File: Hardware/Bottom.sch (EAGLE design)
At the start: 13 parts, among them IC1 SI570, IC2 74LVC74A, X1 MINI-USB-SCHIELD-32005-201

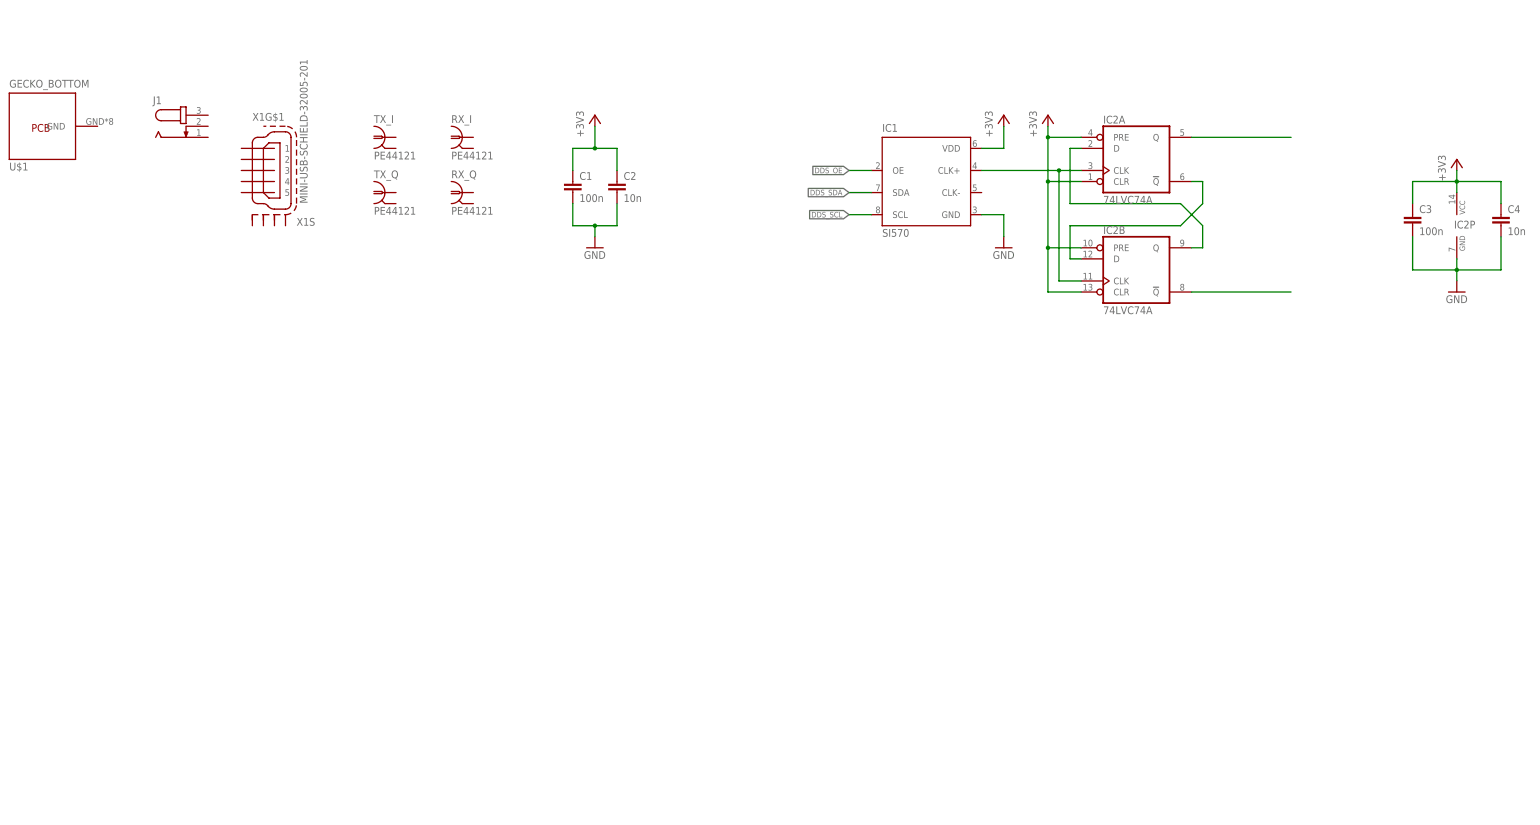
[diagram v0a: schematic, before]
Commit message: Add stepdown converters
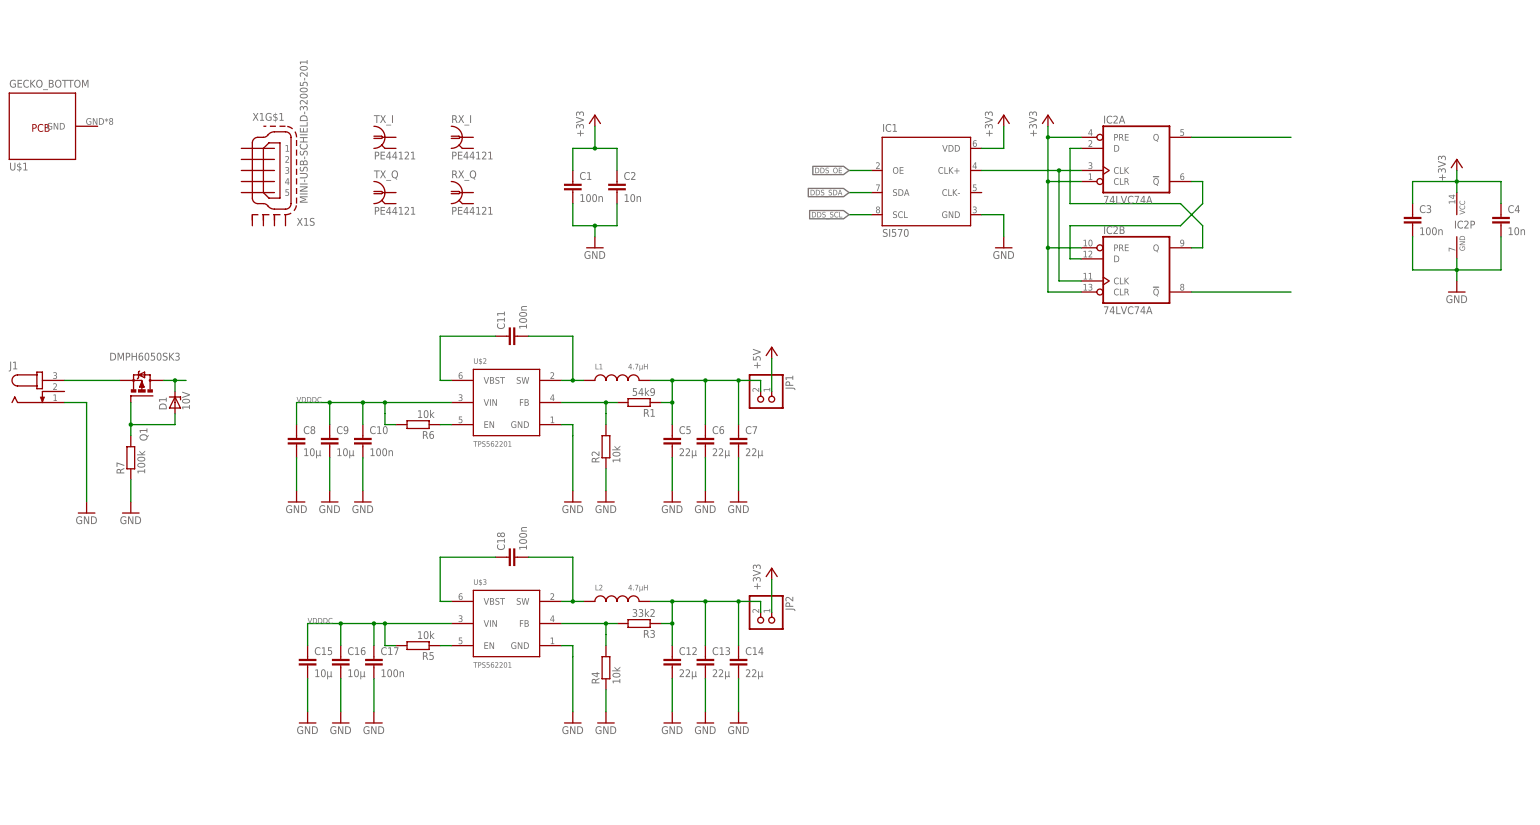
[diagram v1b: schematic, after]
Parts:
- added C10, C11, C17, C18: 100n, rcl:C-EUC0603
- added C12, C13, C14, C5, C6, C7: 22µ, rcl:C-EUC0805
- added C15, C16, C8, C9: 10µ, rcl:C-EUC0805
- added D1: 10V, diode:ZENER-DIODESOT23
- added JP1, JP2: (no value), pinhead:PINHD-1X2
- added L1, L2: 4.7µH, PowerMagnetics (rev18d):WE-MAPI_3020_74438336047
- added Q1: DMPH6050SK3, MyLib:DMP3099L
- added R1: 54k9, rcl:R-EU_R0603
- added R2, R4: 10k, rcl:R-EU_R0603
- added R3: 33k2, rcl:R-EU_R0603
- added R5, R6: 10k, rcl:R-EU_R0402
- added R7: 100k, rcl:R-EU_R0402
- added U$2, U$3: TPS562201, MyLib:TPS562201
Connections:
- new net +5V: JP1.1
- new net N$10: D1.C, Q1.D
- new net N$11: R1.2, R2.2, U$2.FB
- new net N$12: J1.3, Q1.S
- new net N$15: C18.1, U$3.VBST
- new net N$19: C18.2, L2.1, U$3.SW
- new net N$20: R3.2, R4.2, U$3.FB
- new net N$30: C5.1, C6.1, C7.1, JP1.2, L1.2, R1.1
- new net N$31: C12.1, C13.1, C14.1, JP2.2, L2.2, R3.1
- new net N$7: C11.1, U$2.VBST
- new net N$8: C11.2, L1.1, U$2.SW
- new net N$9: D1.A, Q1.G, R7.2
- new net VDDDC: C10.1, C15.1, C16.1, C17.1, C8.1, C9.1, R5.2, R6.2, U$2.VIN, U$3.VIN
- new net VREG_VDD3V3_EN: R5.1, U$3.EN
- new net VREG_VDD5_EN: R6.1, U$2.EN
- net +3V3: now also JP2.1
- net GND: now also C10.2, C12.2, C13.2, C14.2, C15.2, C16.2, C17.2, C5.2, C6.2, C7.2, C8.2, C9.2, J1.1, R2.1, R4.1, R7.1, U$2.GND, U$3.GND
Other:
- moved on the sheet: J1

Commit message: Add sides, add Tayloe Detector
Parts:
- removed RX_I, RX_Q, TX_I, TX_Q: PE44121, con-coax:PE44121
- removed X1: MINI-USB-SCHIELD-32005-201, con-cypressindustries:MINI-USB-SCHIELD-32005-201
- added C19, C20, C21, C26, C27, C31: 100n, rcl:C-EUC0603
- added C22, C23, C24, C25: 4µ7, rcl:C-EUC0805
- added C28: 1µ, rcl:C-EUC0603
- added C29, C30: 2µ, rcl:C-EUC0805
- added C32, C33, C34, C35: (no value), rcl:C-EUC1210
- added C36, C37, C38, C39: (no value), rcl:C-EUC0603
- added IC5: LT6232CGN, linear-technology:LT6232CGN
- added L3, L4: 33µ, rcl:L-EUL3216C
- added R10, R11, R14, R15, R16, R17, R18, R9: (no value), rcl:R-EU_R0603
- added R12, R13: 10k, rcl:R-EU_M0805
- added R8: 10k, rcl:R-EU_R0603
- added RX_IN, RX_IN1: PE44121, con-coax:PE44121
- added SV3, SV4: (no value), con-lstb:MA05-2
- added U$4, U$5: TMUX1511TSSOP14, MyLib:TMUX1511TSSOP14
- added U$6: MABA-007237-ETC410, MyLib:MABA-007237-ETC410
- added U$7: ADS7946, MyLib:ADS7946
- added U$8: MCP1501, MyLib:MCP1501
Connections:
- net DDS_SCL renamed I2C_OSC_SCL
- net DDS_SDA renamed I2C_OSC_SDA
- removed net DDS_OE: IC1.OE
- removed net VDDDC: C10.1, C15.1, C16.1, C17.1, C8.1, C9.1, R5.2, R6.2, U$2.VIN, U$3.VIN
- new net ADC_CHSEL: SV4.1, U$7.CHSEL
- new net I2C_MCS_SCL: SV3.9
- new net I2C_MCS_SDA: SV3.10
- new net N$13: C37.1, IC5D.+IN, R14.2
- new net N$14: IC5A.OUT, R9.1
- new net N$16: C21.1, RX_IN.1
- new net N$17: C21.2, U$6.PD
- new net N$18: C22.1, C23.1, C24.1, C25.1, L3.1, R12.2, U$6.CT
- new net N$21: L3.2, R13.1
- new net N$22: U$4.D1, U$4.D2, U$4.D3, U$4.D4, U$6.SD
- new net N$23: U$5.D1, U$5.D2, U$5.D3, U$5.D4, U$6.S
- new net N$24: C32.1, IC5A.+IN, U$4.S1, U$5.S3
- new net N$25: U$7.A1INP
- new net N$26: U$7.A1INN
- new net N$27: U$7.AREF, U$8.OUT
- new net N$28: U$7.A0INN
- new net N$29: C27.1, C28.1, C29.1, L4.2, U$7.AVDD, U$8.!SHDN, U$8.VDD
- new net N$32: U$7.A0INP
- new net N$33: C33.1, IC5B.+IN, U$4.S2, U$5.S4
- new net N$34: C34.1, IC5A.-IN, U$4.S3, U$5.S1
- new net N$35: SV4.10
- new net N$36: SV4.8
- new net N$37: SV4.6
- new net N$38: SV4.4
- new net N$39: C35.1, IC5B.-IN, U$4.S4, U$5.S2
- new net N$40: C38.1, R10.1, R9.2
- new net N$41: C36.1, IC5C.+IN, R10.2
- new net N$42: C38.2, IC5C.OUT, R18.1
- new net N$43: C39.2, IC5D.OUT, R16.1
- new net N$44: IC5D.-IN, R15.2, R16.2
- new net N$45: IC5C.-IN, R17.2, R18.2
- new net N$6: IC5B.OUT, R11.1
- new net RESV_NC: SV4.2
- new net SPI_ADC_MISO: R8.1, U$7.SDO
- new net SPI_MCS_CLK: SV4.9, U$7.SCLK
- new net SPI_MCS_CS: SV4.3, U$7.!CS
- new net SPI_MCS_MISO: R8.2, SV4.5
- new net SPI_MCS_MOSI: SV4.7
- new net VDD_DC: C10.1, C15.1, C16.1, C17.1, C8.1, C9.1, D1.C, Q1.D, R5.2, R6.2, U$2.VIN, U$3.VIN
- net +3V3: now also C19.1, C20.1, C30.1, C31.1, R13.2, SV3.6, SV3.8, U$4.VCC, U$5.VCC, U$7.DVDD
- net +5V: now also C26.1, IC5P.V+, SV3.2, SV3.4
- net GND: now also C19.2, C20.2, C22.2, C23.2, C24.2, C25.2, C26.2, C27.2, C28.2, C29.2, C30.2, C31.2, C32.2, C33.2, C34.2, C35.2, C36.2, C37.2, IC5P.V-, R12.1, R15.1, R17.1, RX_IN.2, RX_IN1.2, SV3.1, SV3.3, SV3.5, SV3.7, U$4.GND, U$5.GND, U$6.P, U$7.GND, U$7.NC@1, U$7.NC@2, U$7.PDEN, U$7.REFGND, U$8.GND@1, U$8.GND@2, U$8.GND@3
- net N$10: now also C39.1, R11.2, R14.1; no longer D1.C, Q1.D
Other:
- note added: "ECH-U1H153GX5 15nF PPS Film"

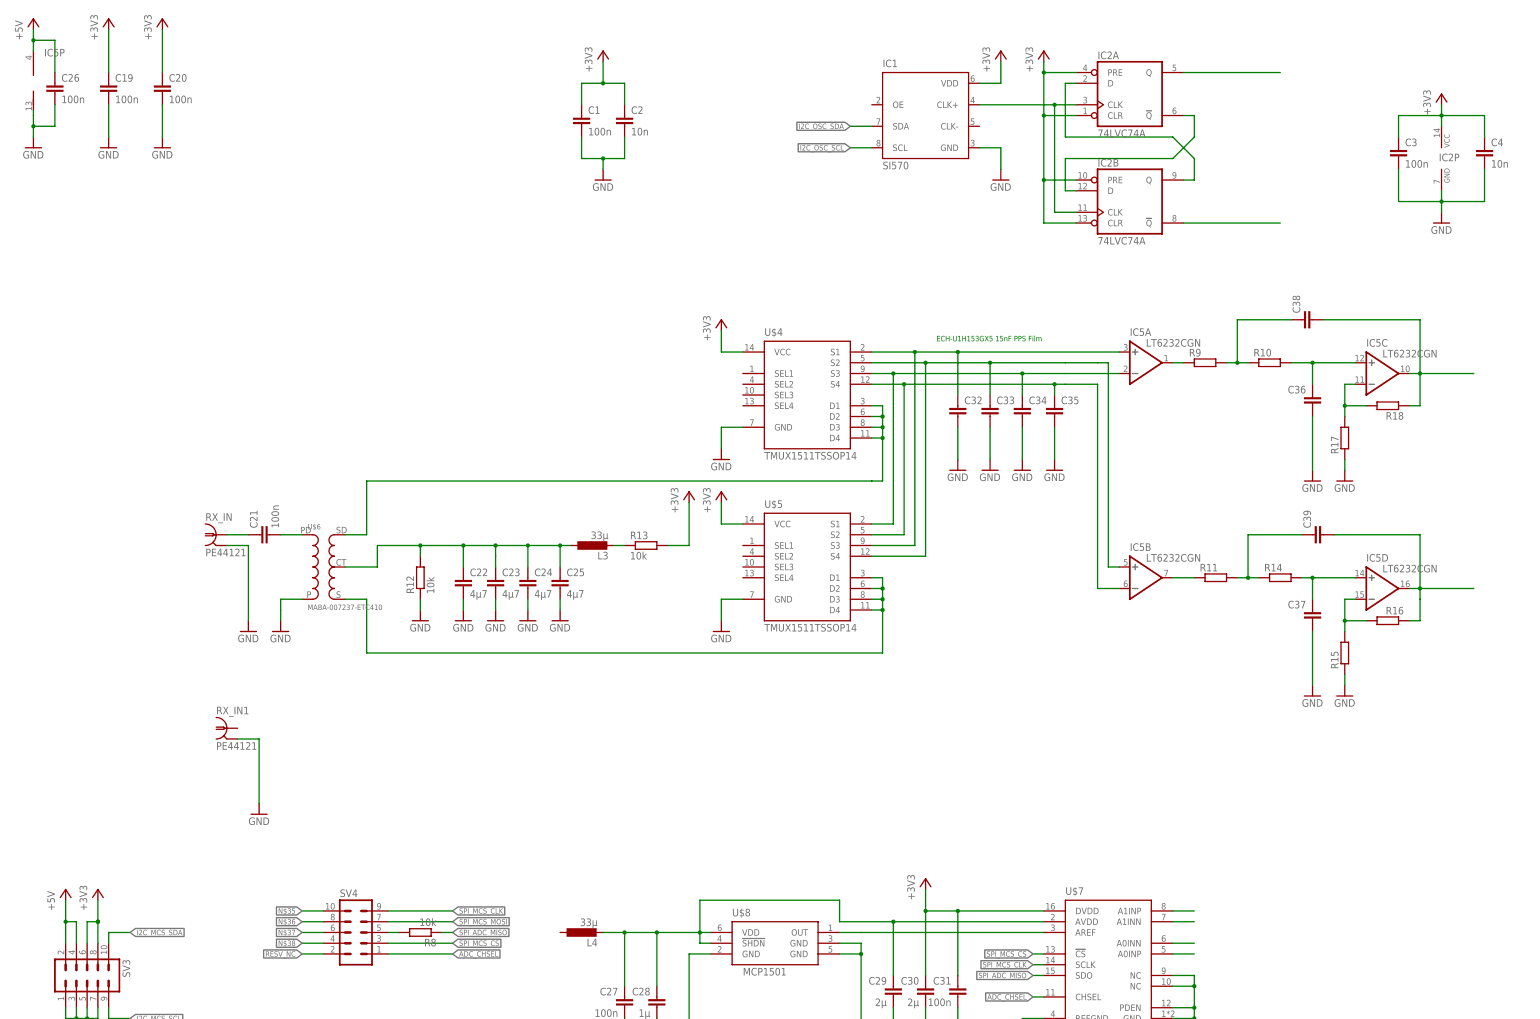
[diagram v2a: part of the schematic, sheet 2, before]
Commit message: Adds SN74CBT3253 to Bottom
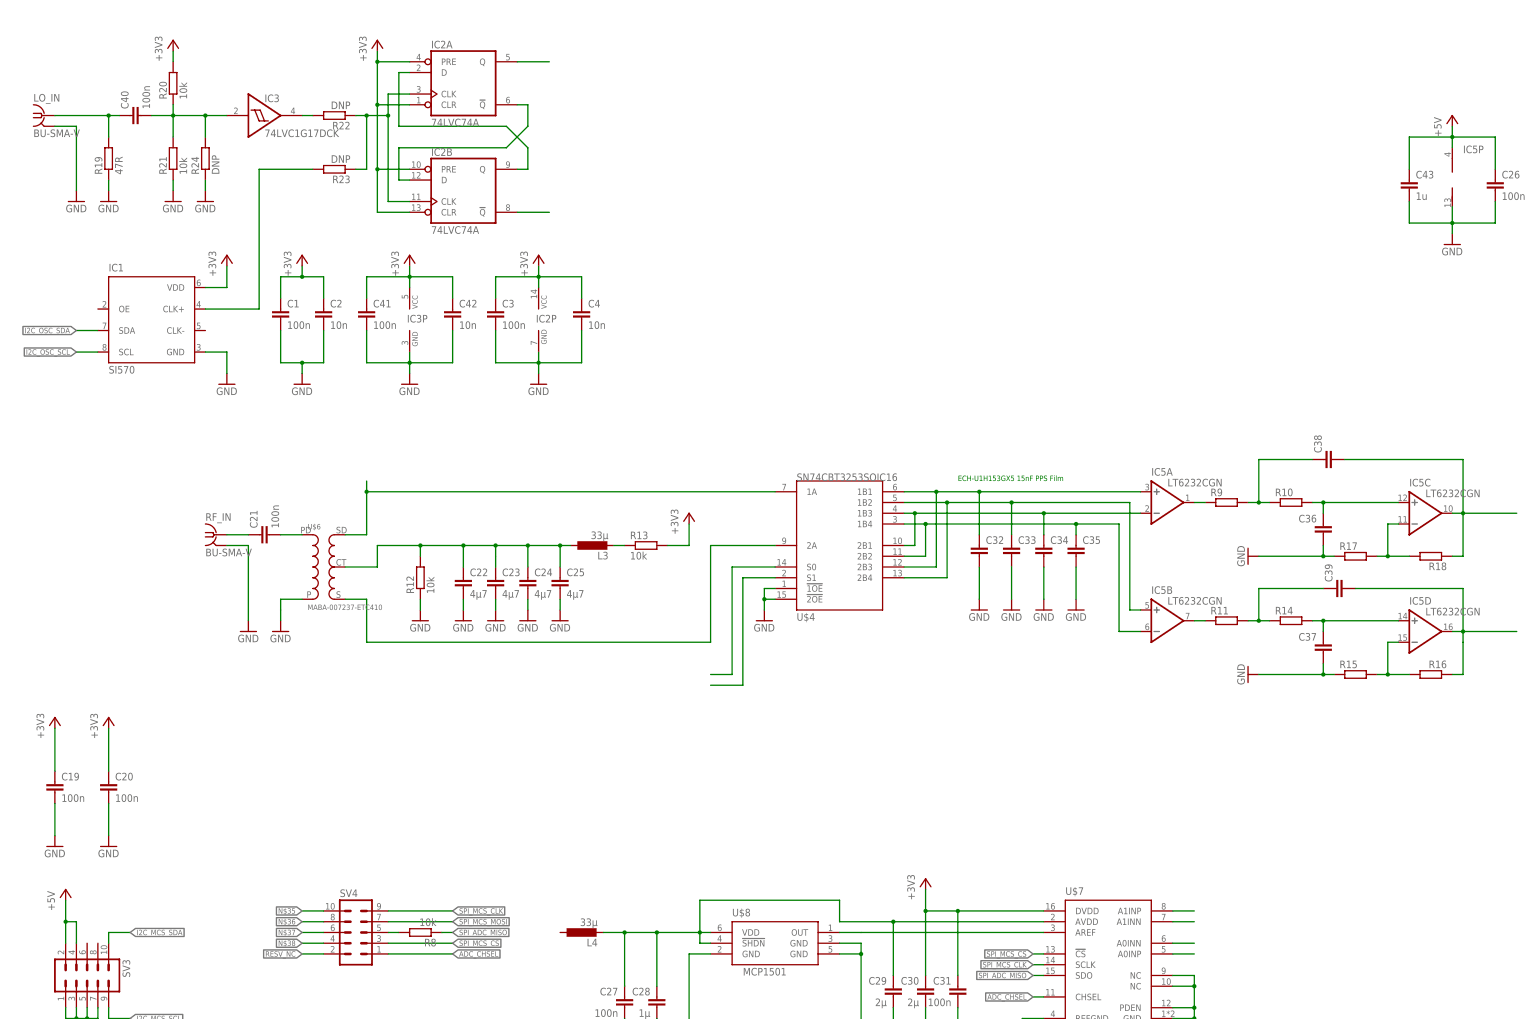
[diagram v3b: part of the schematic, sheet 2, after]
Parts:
- removed RX_IN, RX_IN1: PE44121, con-coax:PE44121
- removed U$5: TMUX1511TSSOP14, MyLib:TMUX1511TSSOP14
- added C40, C41: 100n, rcl:C-EUC0402
- added C42: 10n, rcl:C-EUC0402
- added C43: 1u, rcl:C-EUC0603
- added IC3: 74LVC1G17DCK, 74xx-little-de:74LVC1G17DCK
- added LO_IN, RF_IN: BU-SMA-V, con-coax:BU-SMA-V
- added R19: 47R, rcl:R-EU_R0603
- added R20, R21: 10k, rcl:R-EU_R0603
- added R22, R23, R24: DNP, rcl:R-EU_R0603
- U$4: value TMUX1511TSSOP14 -> SN74CBT3253SOIC16; device MyLib:TMUX1511TSSOP14 -> MyLib:SN74CBT3253SOIC16
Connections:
- removed net N$34: C34.1, IC5A.-IN, U$4.S3, U$5.S1
- new net N$46: C40.1, LO_IN.1, R19.2
- new net N$47: C40.2, IC3G$1.I, R20.1, R21.2, R24.2
- new net N$48: IC3G$1.O, R22.2
- new net N$49: C15.1
- new net N$50: IC1.CLK+, R23.2
- new net N$55: U$4G$1.1A, U$6.SD
- new net N$56: U$4G$1.2A, U$6.S
- new net N$59: C34.1, IC5A.-IN, U$4G$1.1B3, U$4G$1.2B1
- net +3V3: now also C41.1, C42.1, IC3P.VCC, R20.2; no longer SV3.6, SV3.8, U$4.VCC, U$5.VCC
- net +5V: now also C43.1
- net GND: now also C41.2, C42.2, C43.2, IC3P.GND, LO_IN.2, R19.1, R21.1, R24.1, RF_IN.2, U$4G$1.!1OE, U$4G$1.!2OE; no longer RX_IN.2, RX_IN1.2, U$4.GND, U$5.GND
- net N$16: now also RF_IN.1; no longer RX_IN.1
- net N$2: now also R22.1, R23.1; no longer IC1.CLK+
- net N$22: now also U$4G$1.S1; no longer U$4.D1, U$4.D2, U$4.D3, U$4.D4, U$6.SD
- net N$23: now also U$4G$1.S0; no longer U$5.D1, U$5.D2, U$5.D3, U$5.D4, U$6.S
- net N$24: now also U$4G$1.1B1, U$4G$1.2B3; no longer U$4.S1, U$5.S3
- net N$33: now also U$4G$1.1B2, U$4G$1.2B4; no longer U$4.S2, U$5.S4
- net N$39: now also U$4G$1.1B4, U$4G$1.2B2; no longer U$4.S4, U$5.S2
- net VDD_DC: no longer C15.1
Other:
- moved on the sheet: C1, C19, C2, C20, C26, C3, C32, C33, C34, C35, C36, C37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
